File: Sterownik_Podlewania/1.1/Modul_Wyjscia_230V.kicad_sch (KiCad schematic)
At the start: 3 parts, among them J14 Screw_Terminal_01x02

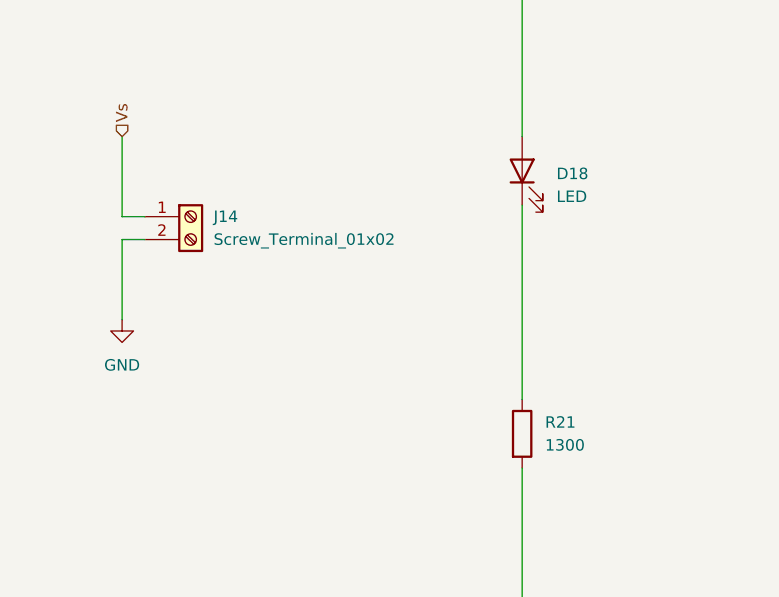
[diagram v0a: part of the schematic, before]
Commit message: Poprawiono błędy połączeń SDA,SCL, dodno drugą magistralę I2C, pociągnięcie nowych ścieżek
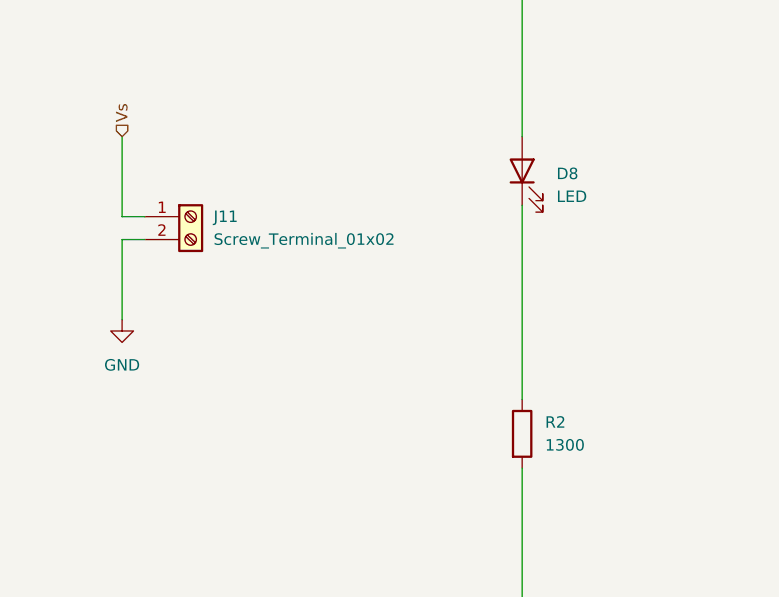
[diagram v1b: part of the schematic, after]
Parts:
- renumbered D18 to D8, J14 to J11, R21 to R2
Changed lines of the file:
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@@
 		(dnp no)
 		(fields_autoplaced yes)
-		(property "Reference" "R21"
+		(property "Reference" "R2"
 			(at 168.91 119.3799 0)
 			(effects
@@
 			(project "Sterownik_Podlewania"
 				(path "/a66bdf1f-0e2a-4cc5-beb1-605f2a3b9885/9a88e80e-3101-4c9e-b6e9-f6fd66520dd2"
-					(reference "R21")
+					(reference "R2")
 					(unit 1)
 				)
@@
 		(dnp no)
 		(fields_autoplaced yes)
-		(property "Reference" "J14"
+		(property "Reference" "J11"
 			(at 132.08 96.5199 0)
 			(effects
@@
 			(project "Sterownik_Podlewania"
 				(path "/a66bdf1f-0e2a-4cc5-beb1-605f2a3b9885/9a88e80e-3101-4c9e-b6e9-f6fd66520dd2"
-					(reference "J14")
+					(reference "J11")
 					(unit 1)
 				)
@@
 		(dnp no)
 		(fields_autoplaced yes)
-		(property "Reference" "D18"
+		(property "Reference" "D8"
 			(at 170.18 91.7574 90)
 			(effects
@@
 			(project "Sterownik_Podlewania"
 				(path "/a66bdf1f-0e2a-4cc5-beb1-605f2a3b9885/9a88e80e-3101-4c9e-b6e9-f6fd66520dd2"
-					(reference "D18")
-					(unit 1)
-				)
+					(reference "D8")
+					(unit 1)
+				)

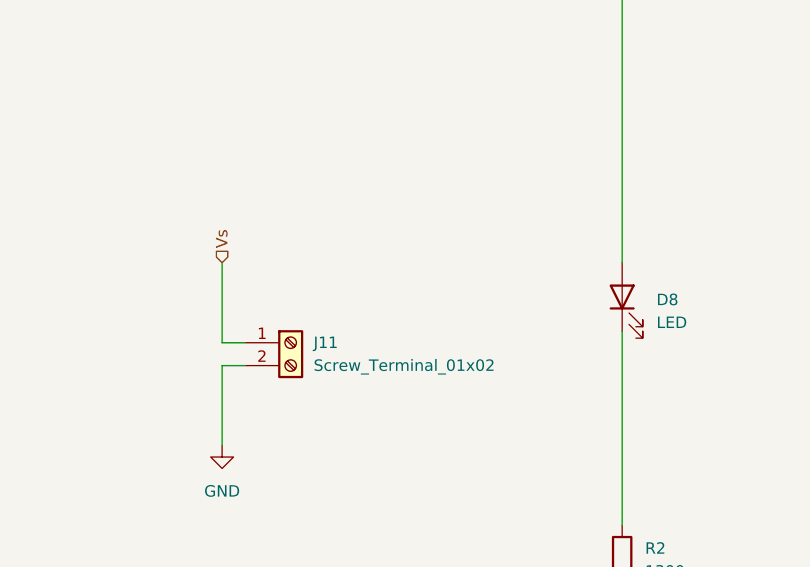
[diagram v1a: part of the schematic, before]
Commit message: Poprawki schematu modułu zaworu, usunięcie przekaźnika, przygotowanie schematu zasilania
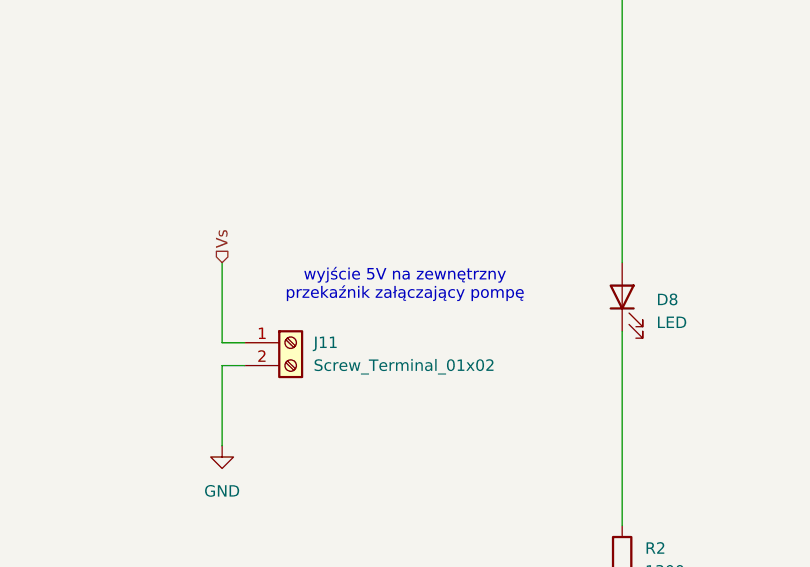
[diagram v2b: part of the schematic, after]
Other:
- note added: "wyjście 5V na zewnętrzny przekaźnik załączający pompę"
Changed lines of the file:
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@@
 		(comment 2 "Filip Gajewski")
+	)
+	(text "wyjście 5V na zewnętrzny \nprzekaźnik załączający pompę"
+		(exclude_from_sim no)
+		(at 142.24 90.17 0)
+		(effects
+			(font
+				(size 1.27 1.27)
+			)
+		)
 	)
 	(text "Vs - sygnał z esp załączający daną sekcję (podniesiony do 5V przez konwerter)\nWł/WYł - stan przełącznika (obsługa manualna)\n"

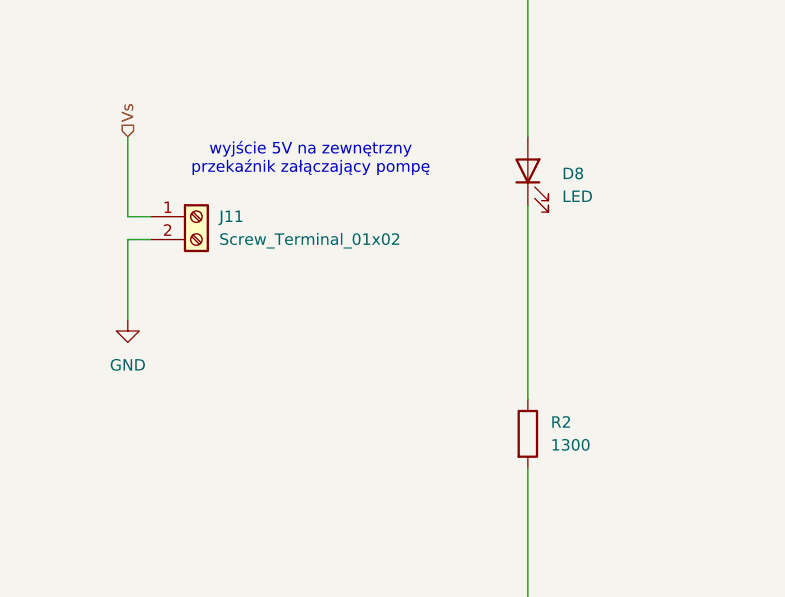
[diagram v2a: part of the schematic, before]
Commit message: Usunięcie zewnętrzego zasilania 12 i stabilizatora napięcia, korekcja zasilania wzmacniacz operacyjny moduł zasilania
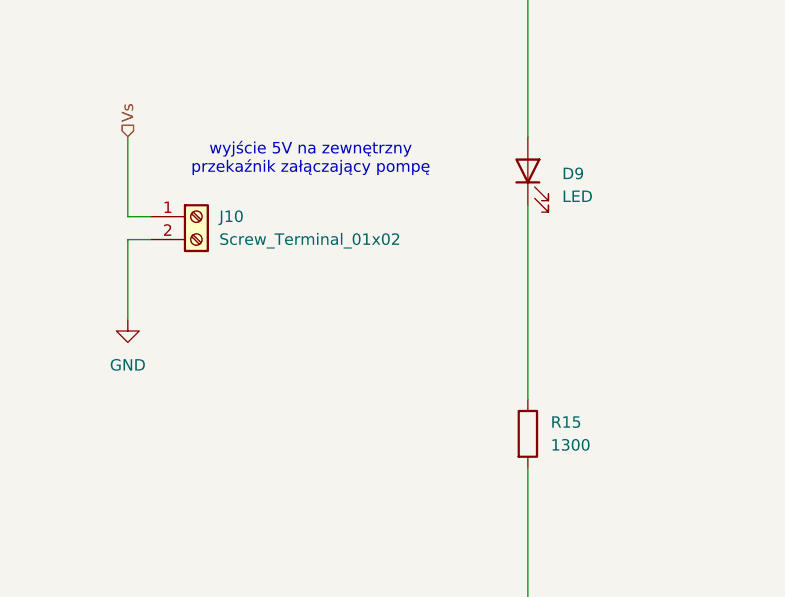
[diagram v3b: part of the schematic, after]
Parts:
- renumbered D8 to D9, J11 to J10, R2 to R15
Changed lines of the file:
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@@
 		(dnp no)
 		(fields_autoplaced yes)
-		(property "Reference" "#PWR055"
+		(property "Reference" "#PWR060"
 			(at 121.92 114.3 0)
 			(effects
@@
 			(project "Sterownik_Podlewania"
 				(path "/a66bdf1f-0e2a-4cc5-beb1-605f2a3b9885/9a88e80e-3101-4c9e-b6e9-f6fd66520dd2"
-					(reference "#PWR055")
+					(reference "#PWR060")
 					(unit 1)
 				)
@@
 		(dnp no)
 		(fields_autoplaced yes)
-		(property "Reference" "R2"
+		(property "Reference" "R15"
 			(at 168.91 119.3799 0)
 			(effects
@@
 			(project "Sterownik_Podlewania"
 				(path "/a66bdf1f-0e2a-4cc5-beb1-605f2a3b9885/9a88e80e-3101-4c9e-b6e9-f6fd66520dd2"
-					(reference "R2")
+					(reference "R15")
 					(unit 1)
 				)
@@
 		(dnp no)
 		(fields_autoplaced yes)
-		(property "Reference" "J11"
+		(property "Reference" "J10"
 			(at 132.08 96.5199 0)
 			(effects
@@
 			(project "Sterownik_Podlewania"
 				(path "/a66bdf1f-0e2a-4cc5-beb1-605f2a3b9885/9a88e80e-3101-4c9e-b6e9-f6fd66520dd2"
-					(reference "J11")
+					(reference "J10")
 					(unit 1)
 				)
@@
 		(dnp no)
 		(fields_autoplaced yes)
-		(property "Reference" "#PWR053"
+		(property "Reference" "#PWR061"
 			(at 166.37 147.32 0)
 			(effects
@@
 			(project "Sterownik_Podlewania"
 				(path "/a66bdf1f-0e2a-4cc5-beb1-605f2a3b9885/9a88e80e-3101-4c9e-b6e9-f6fd66520dd2"
-					(reference "#PWR053")
+					(reference "#PWR061")
 					(unit 1)
 				)
@@
 		(dnp no)
 		(fields_autoplaced yes)
-		(property "Reference" "D8"
+		(property "Reference" "D9"
 			(at 170.18 91.7574 90)
 			(effects
@@
 			(project "Sterownik_Podlewania"
 				(path "/a66bdf1f-0e2a-4cc5-beb1-605f2a3b9885/9a88e80e-3101-4c9e-b6e9-f6fd66520dd2"
-					(reference "D8")
-					(unit 1)
-				)
+					(reference "D9")
+					(unit 1)
+				)

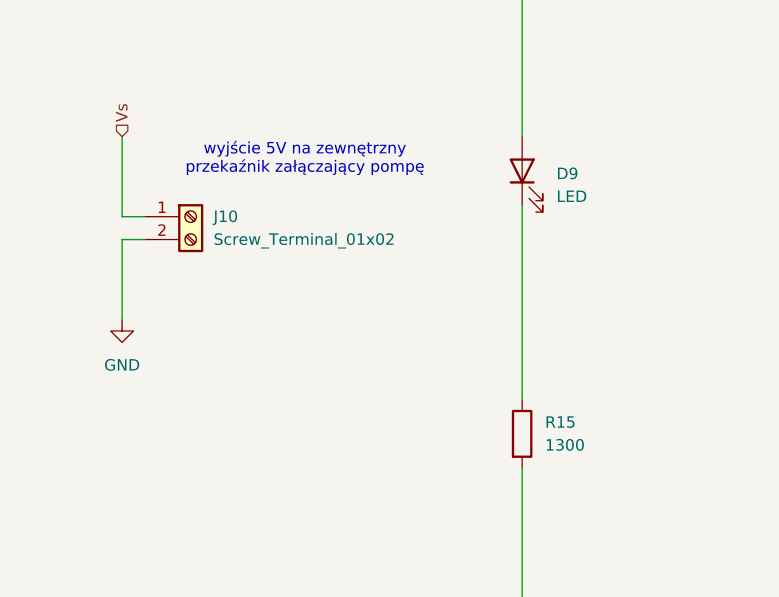
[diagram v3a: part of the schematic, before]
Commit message: Werja plików podesłana Mariuszkowi, dodane opisy i numeracja poprawna dla steronwika, w module poprawniono opis złącze ethernet
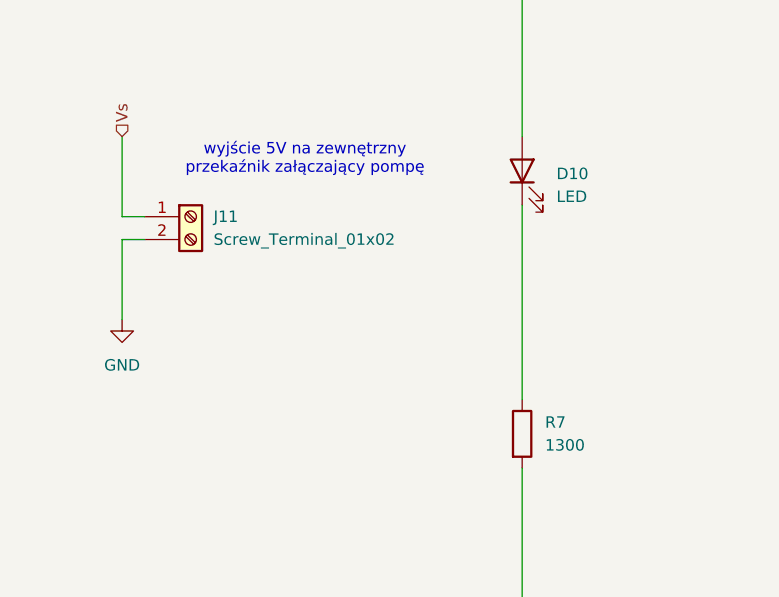
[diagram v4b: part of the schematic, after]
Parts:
- renumbered D9 to D10, J10 to J11, R15 to R7
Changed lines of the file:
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@@
 		(dnp no)
 		(fields_autoplaced yes)
-		(property "Reference" "R15"
+		(property "Reference" "R7"
 			(at 168.91 119.3799 0)
 			(effects
@@
 			(project "Sterownik_Podlewania"
 				(path "/a66bdf1f-0e2a-4cc5-beb1-605f2a3b9885/9a88e80e-3101-4c9e-b6e9-f6fd66520dd2"
-					(reference "R15")
+					(reference "R7")
 					(unit 1)
 				)
@@
 		(dnp no)
 		(fields_autoplaced yes)
-		(property "Reference" "J10"
+		(property "Reference" "J11"
 			(at 132.08 96.5199 0)
 			(effects
@@
 			(project "Sterownik_Podlewania"
 				(path "/a66bdf1f-0e2a-4cc5-beb1-605f2a3b9885/9a88e80e-3101-4c9e-b6e9-f6fd66520dd2"
-					(reference "J10")
+					(reference "J11")
 					(unit 1)
 				)
@@
 		(dnp no)
 		(fields_autoplaced yes)
-		(property "Reference" "D9"
+		(property "Reference" "D10"
 			(at 170.18 91.7574 90)
 			(effects
@@
 			(project "Sterownik_Podlewania"
 				(path "/a66bdf1f-0e2a-4cc5-beb1-605f2a3b9885/9a88e80e-3101-4c9e-b6e9-f6fd66520dd2"
-					(reference "D9")
-					(unit 1)
-				)
+					(reference "D10")
+					(unit 1)
+				)

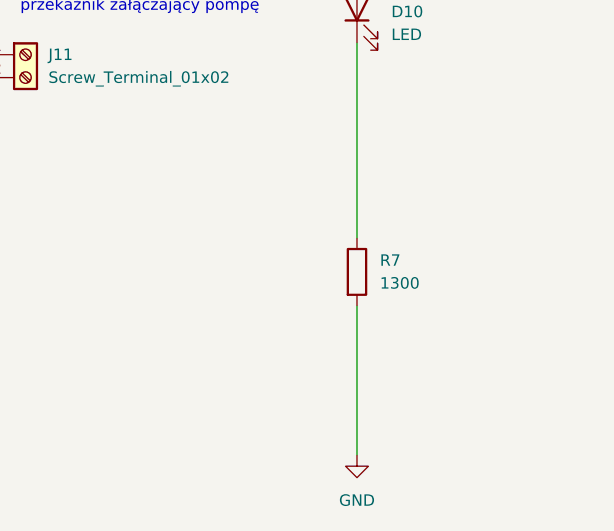
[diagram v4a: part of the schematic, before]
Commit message: Kod websocket, kod stonka demo, kod sterownika - wszystkie taski poza bt wstepnie ogarniete
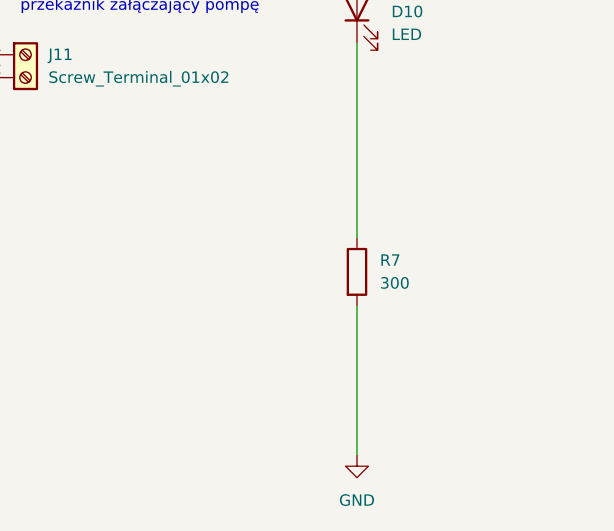
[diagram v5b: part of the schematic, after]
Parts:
- R7: value 1300 -> 300
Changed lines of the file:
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@@
 			)
 		)
-		(property "Value" "1300"
+		(property "Value" "300"
 			(at 168.91 121.9199 0)
 			(effects
